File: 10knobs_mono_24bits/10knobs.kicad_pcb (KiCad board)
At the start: 2 copper layers, 42 parts, among them J1 Conn_01x06_Female, U1 MCP4822, U2 BluePill_STM32F103C, U3 6N138, U4 LM358

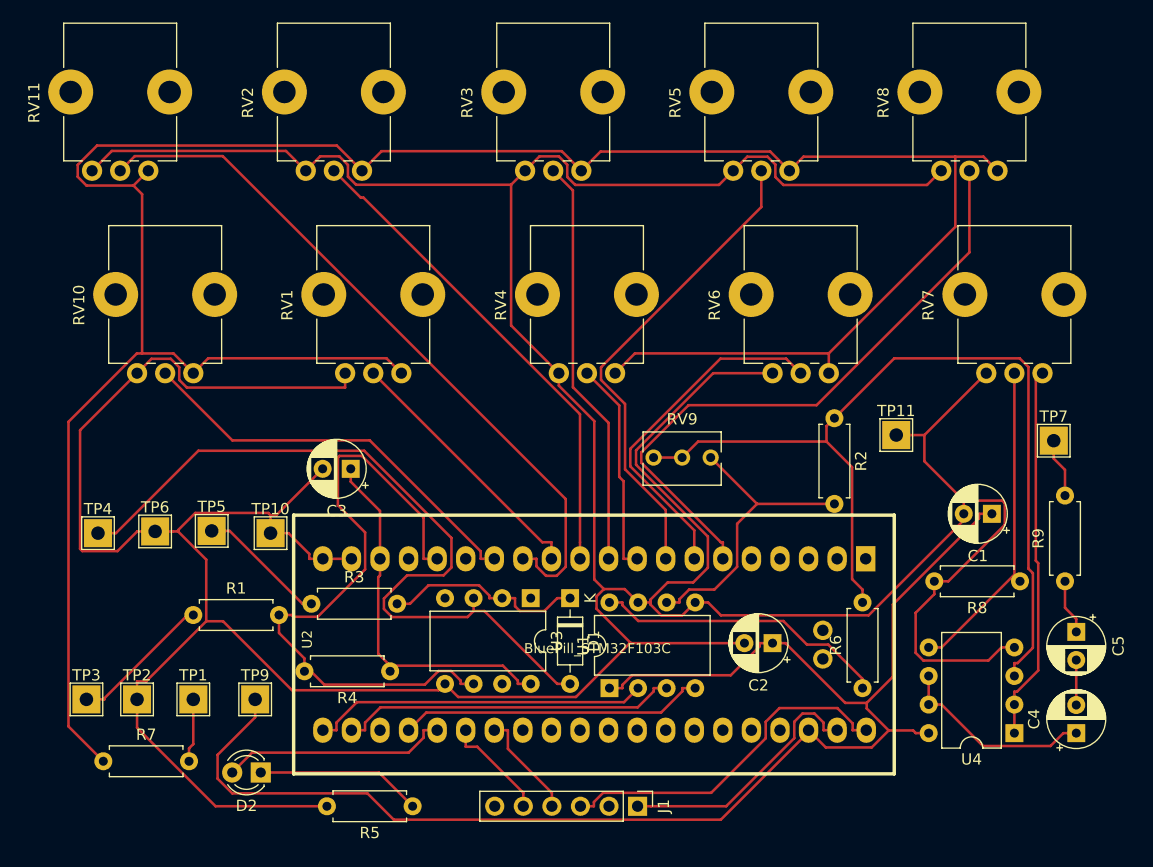
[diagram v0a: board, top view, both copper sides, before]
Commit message: Added PCB, final corrections
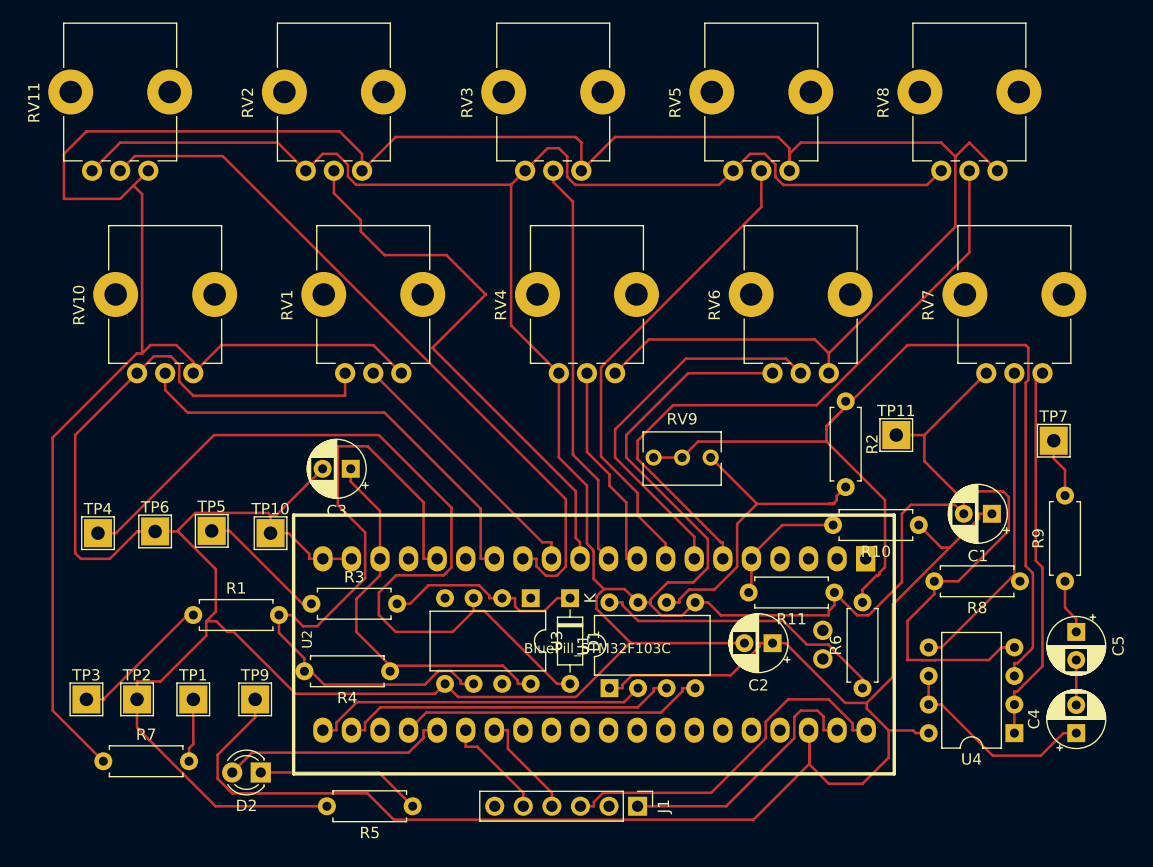
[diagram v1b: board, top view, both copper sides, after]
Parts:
- added R10: 22k, Resistor_THT:R_Axial_DIN0207_L6.3mm_D2.5mm_P7.62mm_Horizontal, F.Cu at (124.0, 70.5)
- added R11: 22k, Resistor_THT:R_Axial_DIN0207_L6.3mm_D2.5mm_P7.62mm_Horizontal, F.Cu at (116.5, 76.5)
- J1: value Conn_01x06_Female -> 3.3 GND
- moved R2 1.80 mm to (117.5, 59.5)
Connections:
- U2 pad 5: (no net) -> Net-(R10-Pad2)
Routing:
- net +3V3: track 219.8 -> 238.9 mm
- net GND: track 421.9 -> 440.3 mm
- net Net-(R10-Pad2): track 0.00 -> 11.8 mm
- net Net-(C1-Pad1): track 130.3 -> 141.4 mm
- net Net-(RV2-Pad2): track 43.7 -> 50.7 mm
- net Net-(R2-Pad1): track 82.2 -> 89.1 mm
- net Net-(D1-Pad2): track 69.3 -> 74.6 mm
- net Net-(R1-Pad2): track 58.1 -> 61.3 mm
- net Net-(RV10-Pad2): track 36.5 -> 39.6 mm
- net Net-(RV6-Pad2): track 31.1 -> 34.1 mm
- net Net-(R2-Pad2): track 26.8 -> 29.1 mm
- net Net-(C3-Pad1): track 32.9 -> 34.5 mm
- net Net-(RV8-Pad2): track 56.4 -> 57.4 mm
- net Net-(J1-Pad1): track 23.0 -> 23.8 mm
- net Net-(C4-Pad1): track 17.7 -> 18.4 mm
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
